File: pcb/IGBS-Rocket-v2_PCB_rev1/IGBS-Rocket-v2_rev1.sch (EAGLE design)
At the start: 250 parts, among them IC1 NCV21872DR2G, IC2 NCV21872DR2G, IC3 NCV21872DR2G, Q1 BC817, Q2 ENC-03, Q3 BSS316N, Q4 BC817, Q5 BSS314PE, U1 STM32H750VBT6, U2 LM317BD2TG, U3 CS5171EDR8G, U5 MICROSD, U6 ESP-12E/F, U8 LP324DRG4, U9 MCP6V51T-E/MS, Y1 24MHz

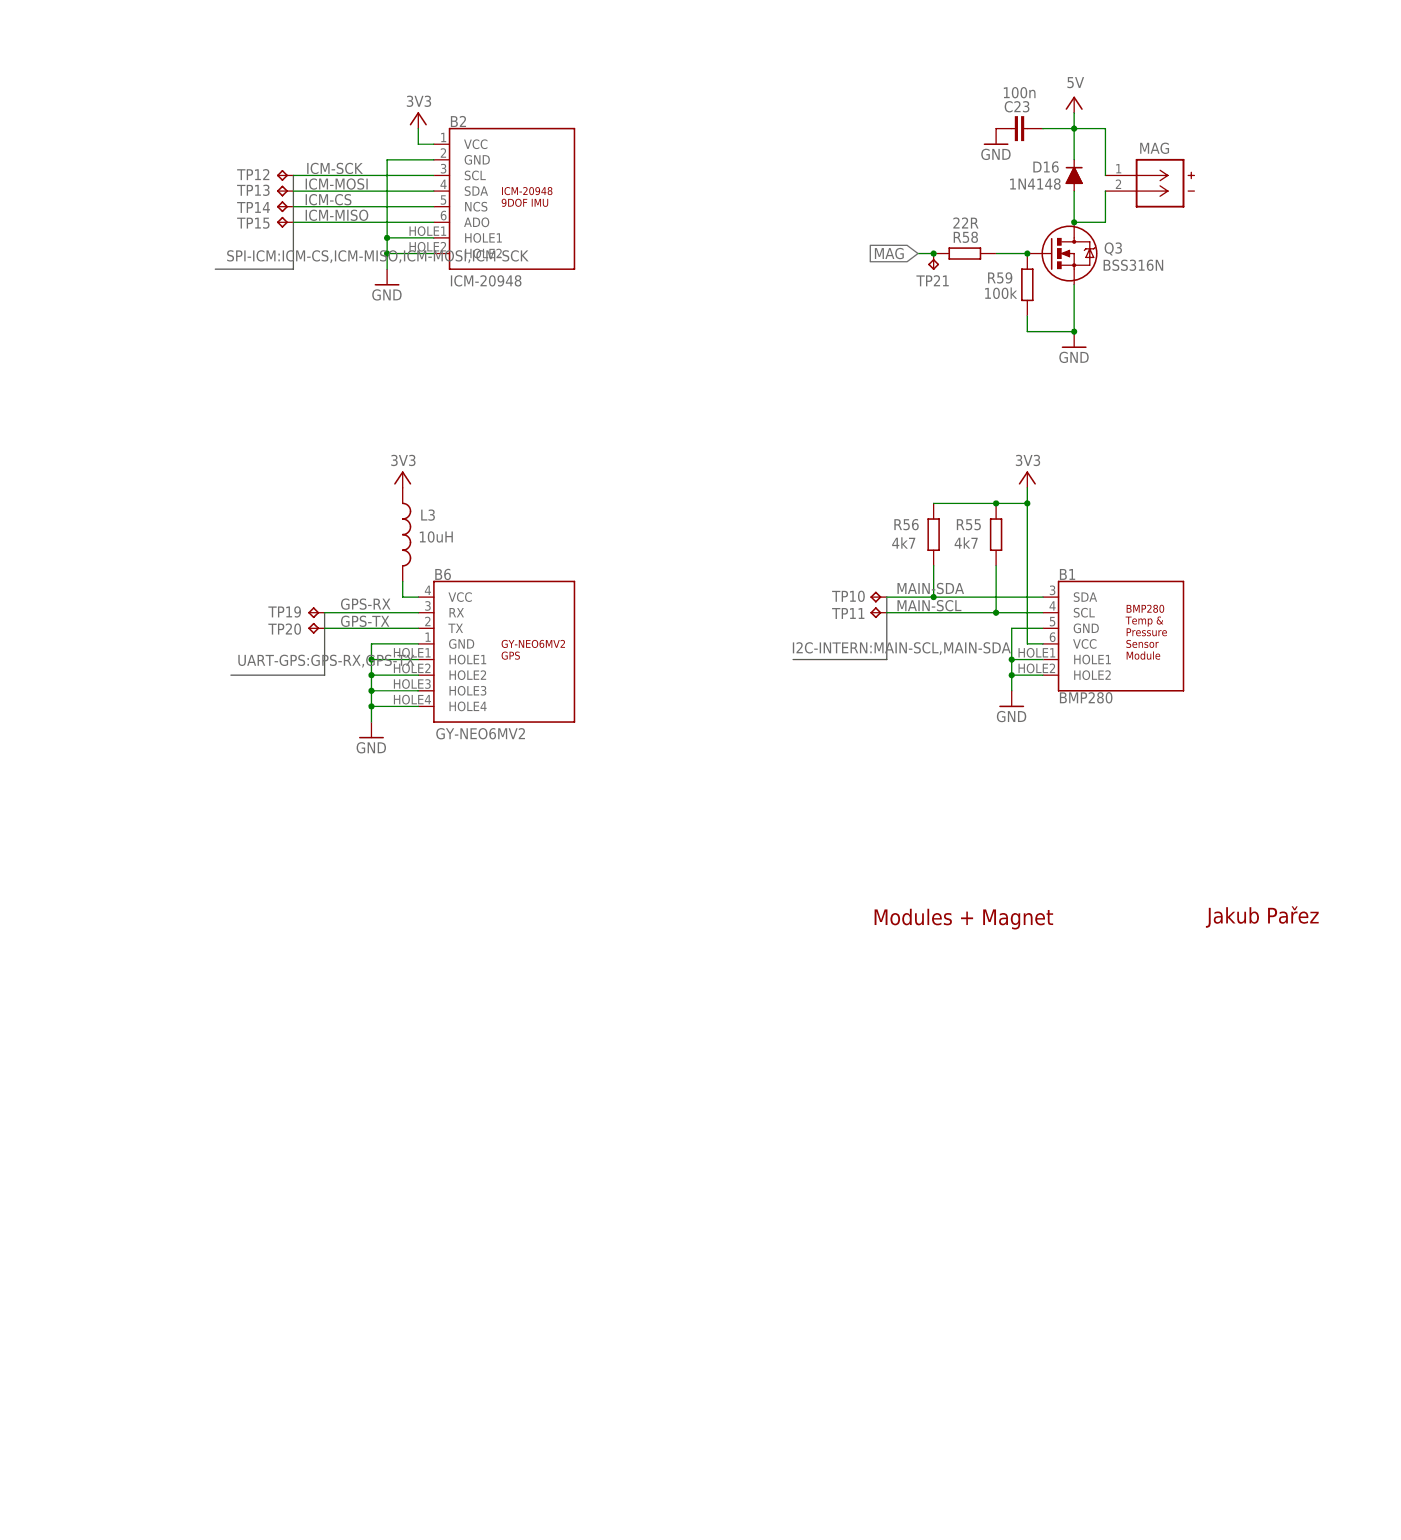
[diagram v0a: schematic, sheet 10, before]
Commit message: * PCB schematics upgrade (removed all modules) last thing GPS part needs to be done
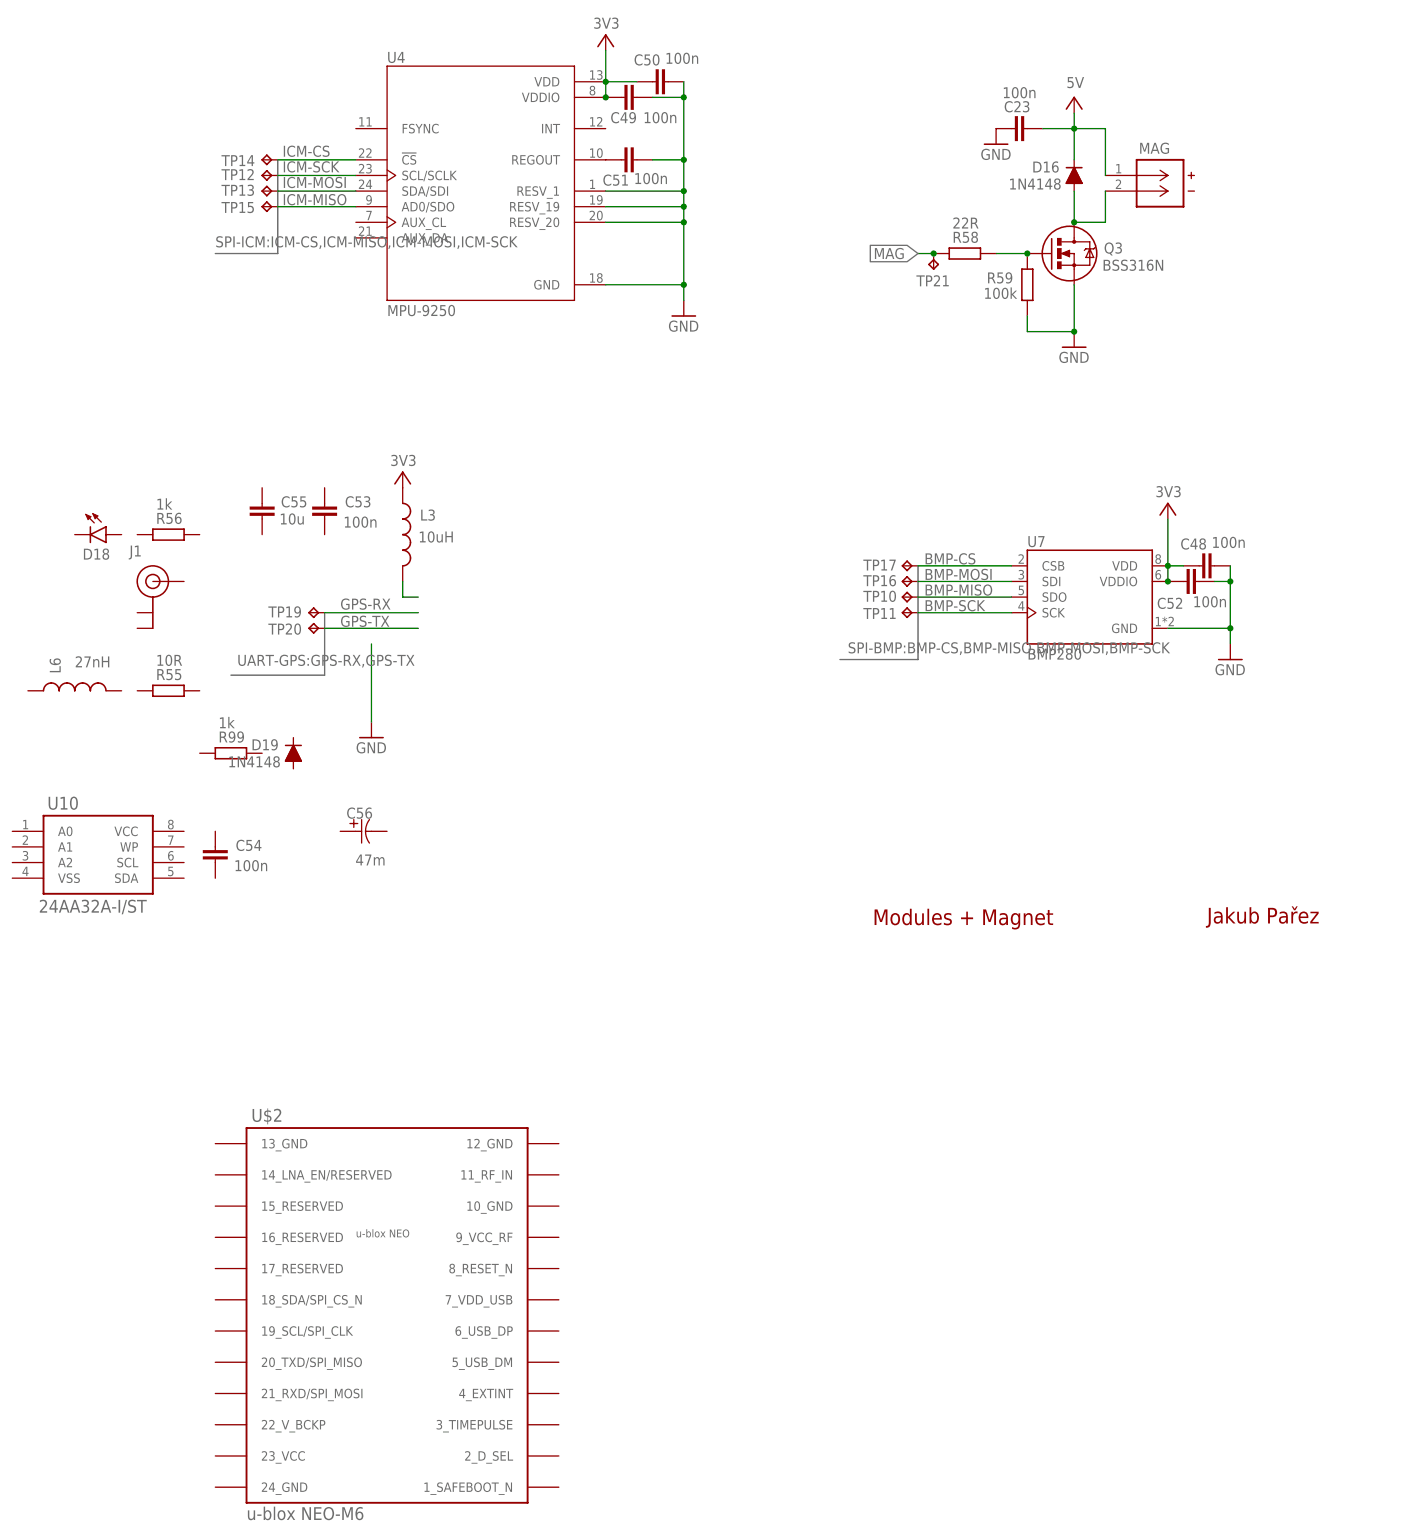
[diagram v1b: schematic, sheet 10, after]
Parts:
- removed B1: BMP280, modules:BMP280-LESSPINS
- removed B2: ICM-20948, modules:ICM-20948-LESSPINS
- removed B6: GY-NEO6MV2, modules:GY-NEO6MV2
- added C48, C49, C50, C51, C52, C53, C54: 100n, rcl2:C-EUC0603K
- added C55: 10u, SparkFun-Capacitors:10UF10V10%(0805)
- added C56: 47m, supercap:FC0H473ZFTBR24FC0H473ZFTBR24_KEM
- added D18: GREEN, leds:LED-GREEN1206
- added D19: 1N4148, SparkFun-DiscreteSemi:DIODESOD123
- added J1: U.FL, SparkFun-Connectors:U.FL
- added L6: 27nH, rcl2:INDUCTOR0402
- added R99: 1k, rcl2:R-EU_R0603
- added TP16, TP17: TPB1,27, testpad2:TPB1,27
- added U$2: u-blox NEO-M6, gps:NEO-M8
- added U10: 24AA32A-I/ST, eeprom:24AA32A-I/STTSSOP8_MC_MCH
- added U4: MPU-9250, gyro:MPU-9250
- added U7: BMP280, gyro:BMP280
- R55: value 4k7 -> 10R
- R56: value 4k7 -> 1k
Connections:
- removed net MAIN-SCL: B1.SCL, R55.1, TP11.TP, U1A.PB6
- removed net MAIN-SDA: B1.SDA, R56.1, TP10.TP, U1A.PB7
- new net BMP-CS: TP17.TP, U1A.PE4, U7.CSB
- new net BMP-MISO: TP10.TP, U1A.PE5, U7.SDO
- new net BMP-MOSI: TP16.TP, U1A.PE6, U7.SDI
- new net BMP-SCK: TP11.TP, U1A.PE2, U7.SCK
- new net N$74: C51.2, U4.REGOUT
- net 3V3: now also C48.2, C49.2, C50.2, C52.2, U4.VDD, U4.VDDIO, U7.VDD, U7.VDDIO; no longer B1.VCC, B2.VCC, B6.VCC, R55.2, R56.2
- net BUZZER: now also U1A.PC6; no longer U1A.PE6
- net CTRL-12V: now also U1A.PE1; no longer U1A.PC13
- net GND: now also C48.1, C49.1, C50.1, C51.1, C52.1, U4.GND, U4.RESV_1, U4.RESV_19, U4.RESV_20, U7.GND; no longer B1.GND, B1.HOLE1, B1.HOLE2, B2.GND, B2.HOLE1, B2.HOLE2, B6.GND, B6.HOLE1, B6.HOLE2, B6.HOLE3, B6.HOLE4
- net GPIO-AUX-IN1: now also U1A.PE3; no longer U1A.PE2
- net GPIO-AUX-IN2: now also U1A.PC13; no longer U1A.PE3
- net GPIO-AUX-OUT1: now also U1A.PC14; no longer U1A.PE4
- net GPIO-AUX-OUT2: now also U1A.PC15; no longer U1A.PE5
- net GPS-RX: no longer B6.RX
- net GPS-TX: no longer B6.TX
- net ICM-CS: now also U4.!CS; no longer B2.NCS
- net ICM-MISO: now also U4.AD0/SDO; no longer B2.ADO
- net ICM-MOSI: now also U4.SDA/SDI; no longer B2.SDA
- net ICM-SCK: now also U4.SCL/SCLK; no longer B2.SCL
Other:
- moved on the sheet: R55, R56, TP10, TP11, TP12, TP13, TP14, TP15

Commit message: + PCB layout DONE + PCB 3D model is ready
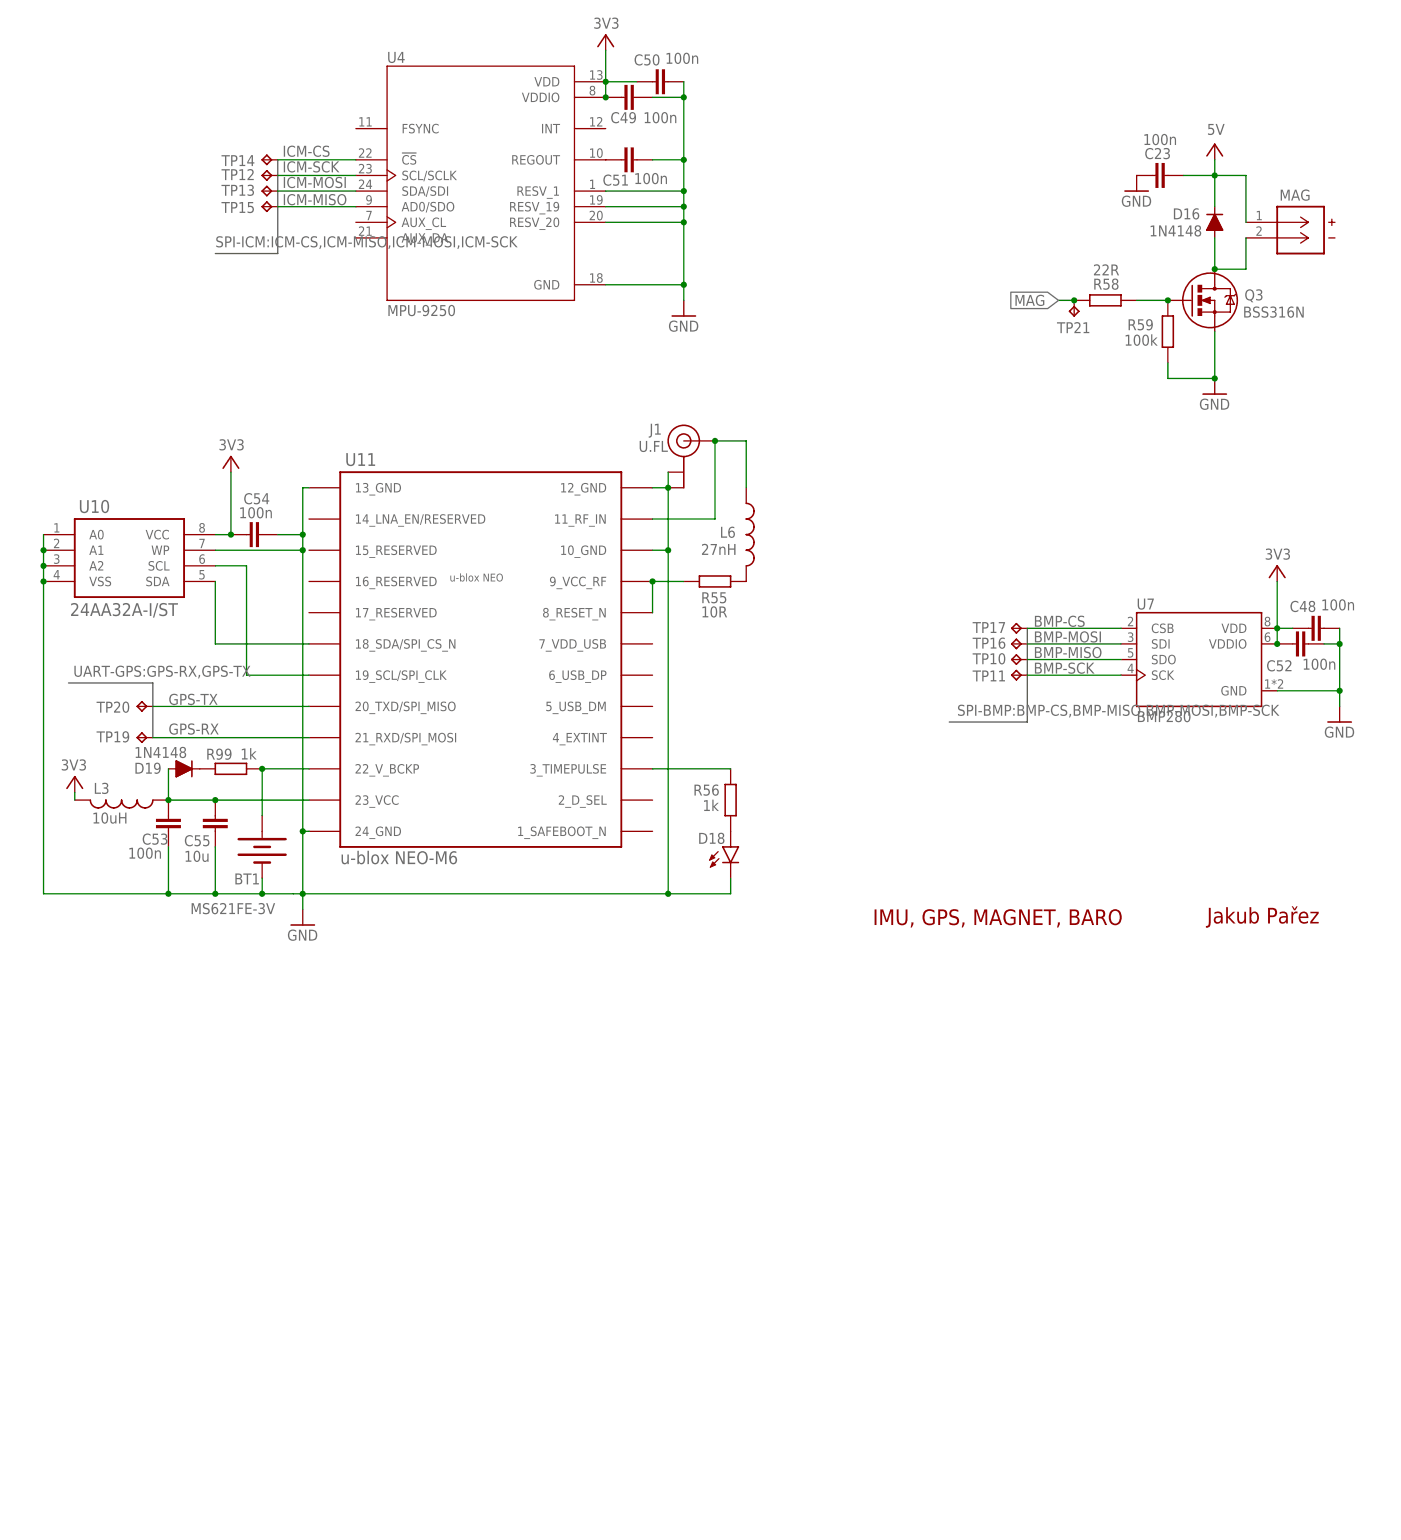
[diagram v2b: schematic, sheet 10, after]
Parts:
- removed C56: 47m, supercap:FC0H473ZFTBR24FC0H473ZFTBR24_KEM
- removed U$2: u-blox NEO-M6, gps:NEO-M8
- added BT1: MS621FE-3V, SparkFun-Batteries:BATTERY-6.8MM_SMD
- added U11: u-blox NEO-M6, gps:NEO-M8
- 3V3-AUX, 5V-AUX, GND-AUX, I2C-AUX, UART-AUX: device pinhead2:PINHD-1X2 -> pinhead2-nopin:PINHD-1X2
- ADC-AUX, SPI-AUX: device pinhead2:PINHD-1X3 -> pinhead2-nopin:PINHD-1X3
- GPIO-AUX: device pinhead2:PINHD-1X4 -> pinhead2-nopin:PINHD-1X4
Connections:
- new net GPS-RF-IN: J1.SIGNAL, L6.1, U11.11_RF_IN
- new net GPS-VBCKP: BT1.+, R99.2, U11.22_V_BCKP
- new net GPS-VCC: C53.1, C55.1, D19.A, L3.1, U11.23_VCC
- new net GPS-VCC-RF: R55.2, U11.8_RESET_N, U11.9_VCC_RF
- new net N$69: U10.SCL, U11.19_SCL/SPI_CLK
- new net N$73: U10.SDA, U11.18_SDA/SPI_CS_N
- new net N$76: D19.C, R99.1
- new net N$78: D18.A, R56.1
- new net N$79: L6.2, R55.1
- new net N$80: R56.2, U11.3_TIMEPULSE
- net GND: now also BT1.-, C53.2, C54.2, C55.2, D18.C, J1.GND@0, J1.GND@1, U10.A0, U10.A1, U10.A2, U10.VSS, U10.WP, U11.10_GND, U11.12_GND, U11.13_GND, U11.24_GND
- net GPS-RX: now also U11.21_RXD/SPI_MOSI
- net GPS-TX: now also U11.20_TXD/SPI_MISO
- net VCC: now also C54.1, U10.VCC; no longer L3.1
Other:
- note added: "IMU, GPS, MAGNET, BARO"
- note added: "IMU/MARG"
- note removed: "9-DOF IMU"
- note removed: "Modules + Magnet"
- moved on the sheet: C23, C48, C52, C53, C54, C55, D16, D18, D19, J1, L3, L6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

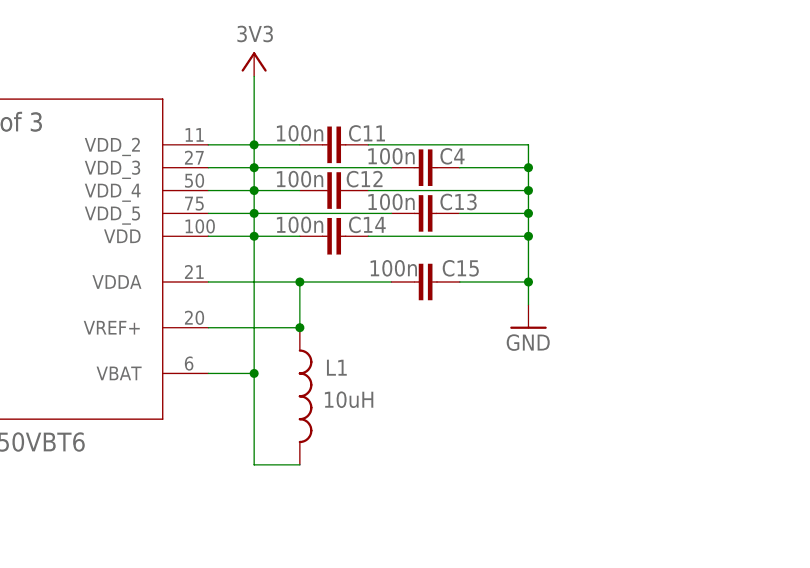
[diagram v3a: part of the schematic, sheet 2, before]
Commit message: + PCB layout checking and cleaning up (silkscreen)
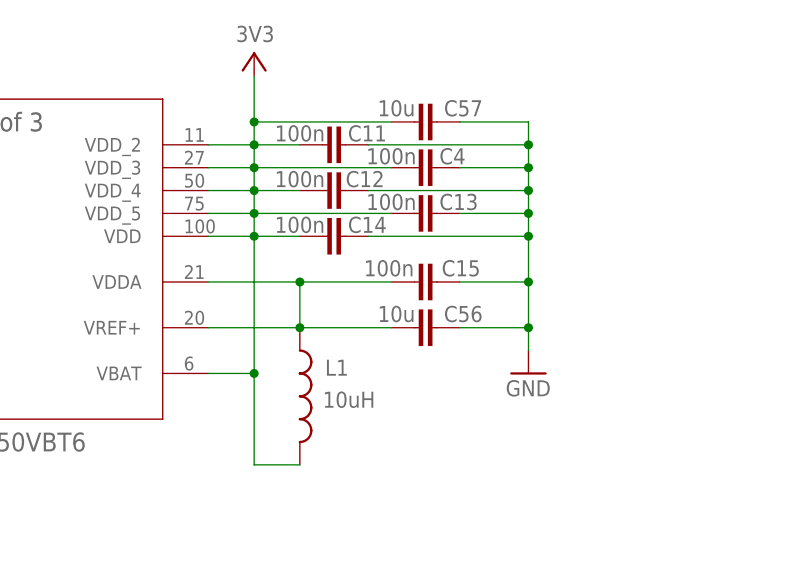
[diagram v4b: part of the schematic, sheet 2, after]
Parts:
- added C56, C57: 10u, SparkFun-Capacitors:10UF10V10%(0805)
- renumbered 3V3-AUX to 3V3, 5V-AUX to 5V, ADC-AUX to ADC, GND-AUX to GND, GPIO-AUX to GPIO, I2C-AUX to I2C, SPI-AUX to SPI, UART-AUX to UART
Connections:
- removed net N$3: C15.2, L1.1, U1C.VDDA, U1C.VREF+
- new net VDDA: C15.2, C56.1, L1.1, U1C.VDDA, U1C.VREF+
- net 3V3: now also C57.1
- net GND: now also C56.2, C57.2
